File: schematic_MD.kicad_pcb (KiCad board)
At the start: 2 copper layers, 100 x 100 mm, 175 parts, among them J1 CAN_Bus, J10 XT60, J2 CAN_Bus, J3 Conn_02x01, J4 Micro_SD_Card_Det2, J5 Conn_02x07_Odd_Even, J6 Rotaly_encoder_1, J7 Rotaly_encoder_2, J8 XT60, J9 XT60, Q1 SQJ886EP-T1_GE3, Q2 SQJ886EP-T1_GE3, Q3 SQJ886EP-T1_GE3, Q4 SQJ886EP-T1_GE3, Q5 SQJ886EP-T1_GE3, Q6 SQJ886EP-T1_GE3, Q7 SQJ886EP-T1_GE3, Q8 SQJ886EP-T1_GE3, SW1 SW_MEC_5G, SW2 SW_DIP_x04, U1 74HC04, U2 MAX3051, U3 STM32F405RGTx, U4 UCC21520DW, U5 UCC21520DW, U6 UCC21520DW, U7 UCC21520DW, U8 TPS54202DDC, U9 XC6206P332MR-G, Y1 25MHz

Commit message: minor change
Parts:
- removed J4: Micro_SD_Card_Det2, RDC_footprint:TF-15
- added C60: 0.1u, Capacitor_SMD:C_0402_1005Metric, F.Cu at (80.9, 70.0)
- added J11: Micro_SD_Card_Det_Hirose_DM3AT, Connector_Card:microSD_HC_Hirose_DM3D-SF, F.Cu at (113.5, 132.8)
- added R62: 10k, Resistor_SMD:R_0402_1005Metric, F.Cu at (78.0, 70.0)
- added R63: 10k, Resistor_SMD:R_0402_1005Metric, F.Cu at (78.0, 72.0)
- moved R55 12.3 mm to (108.2, 124.2)
- moved R61 10.3 mm to (109.2, 124.2)
- moved R51 8.70 mm to (118.2, 124.2)
- moved R56 8.70 mm to (119.2, 124.2)
- moved R54 7.30 mm to (110.2, 124.2)
- moved R60 7.30 mm to (111.2, 124.2)
- moved R57 5.70 mm to (117.2, 124.2)
- moved R52 3.70 mm to (116.2, 124.2)
- moved R53 3.30 mm to (112.2, 124.2)
- moved R59 3.30 mm to (113.2, 124.2)
- moved R58 1.70 mm to (115.2, 124.2)
- moved C59 0.30 mm to (114.2, 124.2)
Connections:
- C16 pad 1: /STM32F405/3.3V_IN -> +3.3V
- C17 pad 1: /STM32F405/3.3V_IN -> +3.3V
- C19 pad 1: /STM32F405/3.3V_IN -> +3.3V
- C21 pad 1: /STM32F405/3.3V_IN -> +3.3V
- C22 pad 1: /STM32F405/3.3V_IN -> +3.3V
- C23 pad 1: /STM32F405/3.3V_IN -> +3.3V
- C52 pad 1: +12V -> /Logic_power/Power_IN
- C53 pad 1: +12V -> /Logic_power/Power_IN
- L1 pad 1: /STM32F405/3.3V_IN -> +3.3V
- SW2 pad 5: /STM32F405/3.3V_IN -> +3.3V
- SW2 pad 6: /STM32F405/3.3V_IN -> +3.3V
- SW2 pad 7: /STM32F405/3.3V_IN -> +3.3V
- SW2 pad 8: /STM32F405/3.3V_IN -> +3.3V
- U3 pad 1: /STM32F405/3.3V_IN -> +3.3V
- U3 pad 19: /STM32F405/3.3V_IN -> +3.3V
- U3 pad 32: /STM32F405/3.3V_IN -> +3.3V
- U3 pad 48: /STM32F405/3.3V_IN -> +3.3V
- U3 pad 64: /STM32F405/3.3V_IN -> +3.3V
- U8 pad 3: +12V -> /Logic_power/Power_IN
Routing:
- net +3.3V: track 127.0 -> 150.9 mm, vias 6 -> 14
- net /STM32F405/3.3V_IN: track 10.5 -> 0.00 mm
- net /STM32F405/D1: track 51.6 -> 58.6 mm
- net /STM32F405/D2: track 51.8 -> 44.8 mm
- net /STM32F405/D0: track 53.8 -> 58.8 mm
- net /STM32F405/D3: track 49.9 -> 45.3 mm
- net /STM32F405/SDCMD: track 47.4 -> 45.4 mm
- net /STM32F405/SDCLK: track 46.0 -> 47.1 mm, vias 4 -> 6
- net Net-(J11-DAT1): track 3.84 -> 4.62 mm
- net GND1: track 70.6 -> 71.1 mm
- net Net-(J11-CMD): track 3.87 -> 4.41 mm

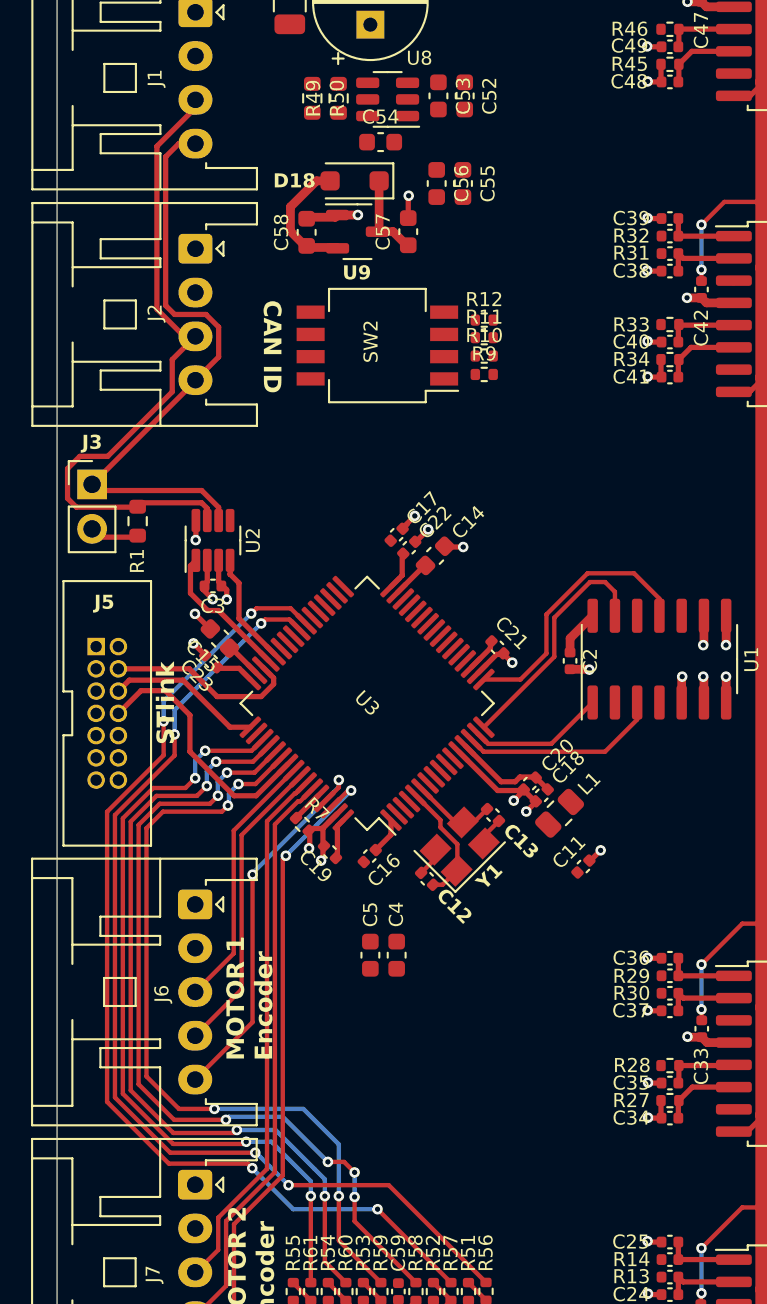
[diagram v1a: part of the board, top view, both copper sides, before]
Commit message: change logic DCDC
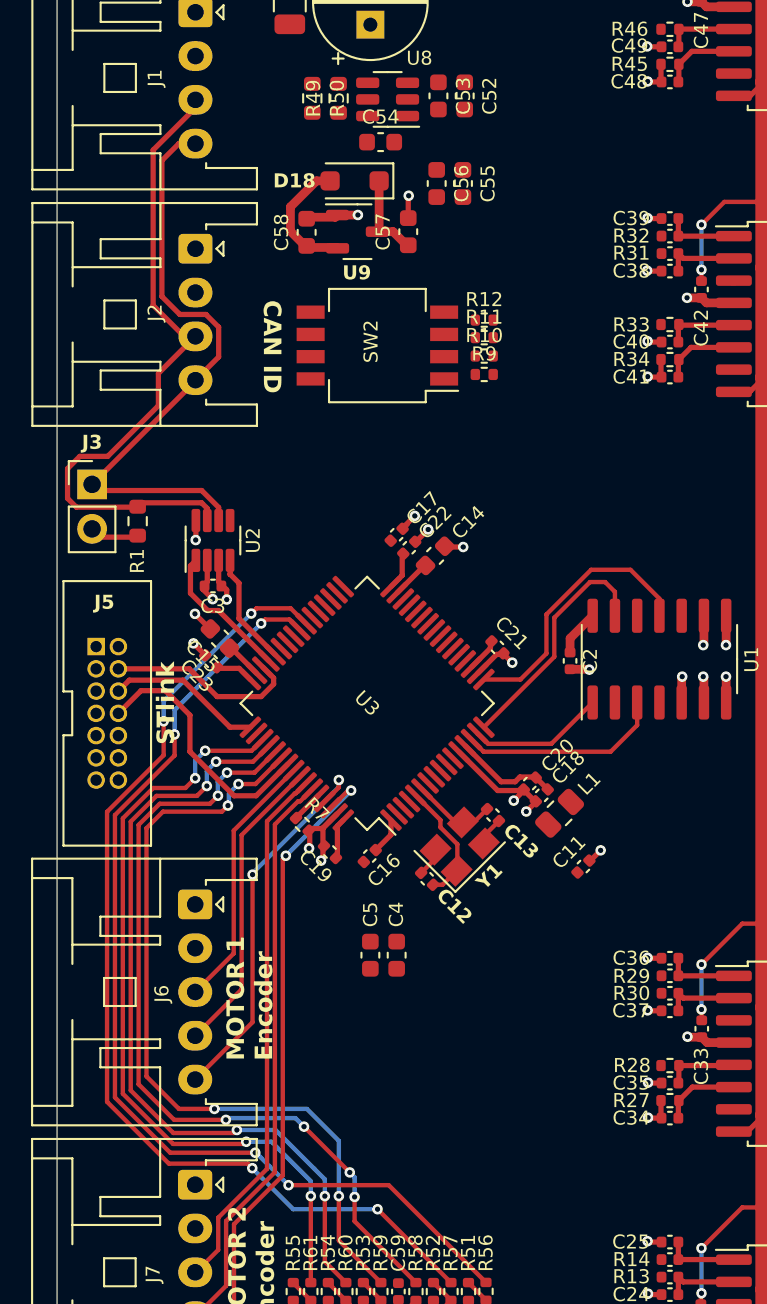
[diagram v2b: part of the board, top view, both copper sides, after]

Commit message: 制御回路完成
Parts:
- added C61: 220u, Capacitor_THT:CP_Radial_D8.0mm_P3.50mm, F.Cu at (141.8, 93.7)
- added C62: 0.1u, Capacitor_SMD:C_0603_1608Metric, F.Cu at (109.8, 113.9)
- added D19: D_Schottky, Diode_SMD:D_SOD-123F, F.Cu at (116.3, 50.9)
- added D20: D_Schottky, Diode_SMD:D_SOD-123F, F.Cu at (138.4, 79.2)
- added L2: 15uH, Inductor_SMD:L_Changjiang_FNR4020S, F.Cu at (118.1, 58.5)
- added L3: 15uH, Inductor_SMD:L_Changjiang_FNR4020S, F.Cu at (140.4, 86.9)
- added Q9: Q_PMOS_GSD, Package_TO_SOT_SMD:SOT-23-3, F.Cu at (109.5, 67.9)
- added R64: 18k, Resistor_SMD:R_0402_1005Metric, F.Cu at (144.2, 85.5)
- added R65: 2k, Resistor_SMD:R_0402_1005Metric, F.Cu at (145.2, 85.5)
- added R66: 10k, Resistor_SMD:R_0402_1005Metric, F.Cu at (120.5, 123.9)
- added R67: 10k, Resistor_SMD:R_0402_1005Metric, F.Cu at (133.2, 133.4)
- added SW3: SW_Push, RDC_footprint:TVBP06-B043, F.Cu at (132.6, 135.8)
- added SW4: SW_SPDT, RDC_footprint:SS-12D, F.Cu at (127.9, 42.8)
- added U10: TPS5430DDA, Package_SO:TI_SO-PowerPAD-8_ThermalVias, F.Cu at (120.3, 52.3)
- C1: value 100u -> 47u; footprint Capacitor_THT:CP_Radial_D6.3mm_P2.50mm -> Capacitor_THT:CP_Radial_D5.0mm_P2.00mm
- C53: value 0.1u -> 220u; footprint Capacitor_SMD:C_0603_1608Metric -> Capacitor_THT:CP_Radial_D8.0mm_P3.50mm
- C54: value 0.1u -> 0.01u
- C55: value 22u -> 10u
- C56: value 22u -> 0.01u
- R49: value 15k -> 12k; footprint Resistor_SMD:R_0603_1608Metric -> Resistor_SMD:R_0402_1005Metric
- R50: value 10k -> 3.9k; footprint Resistor_SMD:R_0603_1608Metric -> Resistor_SMD:R_0402_1005Metric
- SW1: value SW_MEC_5G -> SW_Push
- U8: value TPS54202DDC -> TPS5430DDA; footprint Package_TO_SOT_SMD:SOT-23-6 -> Package_SO:TI_SO-PowerPAD-8_ThermalVias
- moved R12 48.0 mm to (117.4, 116.7), turned to -90 degrees
- moved R11 47.0 mm to (116.4, 116.7), turned to -90 degrees
- moved R10 46.1 mm to (115.3, 116.7), turned to -90 degrees
- moved R9 45.1 mm to (114.3, 116.7), turned to -90 degrees
- moved SW2 40.5 mm to (115.9, 110.6), turned to 90 degrees
- moved U8 37.9 mm to (142.4, 80.8), turned to 90 degrees
- moved R62 31.9 mm to (109.9, 70.7), turned to 90 degrees
- moved C56 31.5 mm to (138.1, 83.8), turned to 0 degrees
- moved R63 30.9 mm to (108.9, 70.7), turned to -90 degrees
- moved C55 28.9 mm to (142.4, 76.2), turned to 0 degrees
- moved C60 27.0 mm to (107.9, 70.7), turned to -90 degrees
- moved D18 15.8 mm to (119.3, 74.6), turned to 0 degrees
- moved C58 15.3 mm to (122.0, 71.7), turned to -90 degrees
- moved R2 14.7 mm to (109.7, 65.0), turned to 180 degrees
- moved R50 13.3 mm to (122.5, 57.1)
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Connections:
- C1 pad 1: +12V -> /Logic_power/Power_IN
- C2 pad 1: gate_logic_PWR -> +3.3V
- C53 pad 1: /Logic_power/Power_IN -> +5V
- C54 pad 1: Net-(U8-BOOT) -> Net-(U10-BOOT)
- C54 pad 2: +5V -> Net-(D19-K)
- C55 pad 1: +5V -> Vdrive
- C55 pad 2: GND1 -> GND2
- C56 pad 1: +5V -> Net-(U8-BOOT)
- C56 pad 2: GND1 -> Net-(D20-K)
- H1 pad 1: GND1 -> unconnected-(H1-Pad1)
- H2 pad 1: GND1 -> unconnected-(H2-Pad1)
- H3 pad 1: GND2 -> unconnected-(H3-Pad1)
- H4 pad 1: GND2 -> unconnected-(H4-Pad1)
- J11 pad 10: unconnected-(J11-DET_A-Pad10) -> SD_Detect
- J11 pad 9: unconnected-(J11-DET_B-Pad9) -> +3.3V
- R10 pad 1: Net-(U3-PB14) -> /STM32F405/CAN_ID2
- R11 pad 1: Net-(U3-PB13) -> /STM32F405/CAN_ID3
- R12 pad 1: Net-(U3-PB12) -> /STM32F405/CAN_ID4
- R2 pad 1: +12V -> /Logic_power/Power_IN
- R49 pad 2: Net-(U8-FB) -> Net-(U10-VSENSE)
- R50 pad 1: Net-(U8-FB) -> Net-(U10-VSENSE)
- R62 pad 2: GND1 -> Net-(SW4-B)
- R8 pad 1: Net-(U3-PA10) -> Net-(U3-PB12)
- R9 pad 1: Net-(U3-PB15) -> /STM32F405/CAN_ID1
- SW2 pad 1: Net-(U3-PB15) -> /STM32F405/CAN_ID1
- SW2 pad 2: Net-(U3-PB14) -> /STM32F405/CAN_ID2
- SW2 pad 3: Net-(U3-PB13) -> /STM32F405/CAN_ID3
- SW2 pad 4: Net-(U3-PB12) -> /STM32F405/CAN_ID4
- U1 pad 14: gate_logic_PWR -> +3.3V
- U1 pad 5: GND1 -> /STM32F405/ENABLE_1
- U1 pad 6: GND1 -> /Driver/EN_left
- U1 pad 8: GND1 -> /Driver1/EN_left
- U1 pad 9: GND1 -> /STM32F405/ENABLE_2
- U3 pad 10: unconnected-(U3-PC2-Pad10) -> /STM32F405/CAN_ID2
- U3 pad 11: unconnected-(U3-PC3-Pad11) -> /STM32F405/CAN_ID1
- U3 pad 20: unconnected-(U3-PA4-Pad20) -> SD_Detect
- U3 pad 21: unconnected-(U3-PA5-Pad21) -> Net-(U3-PA5)
- U3 pad 24: /Driver/EN_left -> /STM32F405/ENABLE_1
- U3 pad 25: /Driver1/EN_left -> /STM32F405/ENABLE_2
- U3 pad 34: Net-(U3-PB13) -> unconnected-(U3-PB13-Pad34)
- U3 pad 35: Net-(U3-PB14) -> unconnected-(U3-PB14-Pad35)
- U3 pad 36: Net-(U3-PB15) -> unconnected-(U3-PB15-Pad36)
- U3 pad 43: Net-(U3-PA10) -> unconnected-(U3-PA10-Pad43)
- U3 pad 8: unconnected-(U3-PC0-Pad8) -> /STM32F405/CAN_ID4
- U3 pad 9: unconnected-(U3-PC1-Pad9) -> /STM32F405/CAN_ID3
- U8 pad 1: GND1 -> Net-(U8-BOOT)
- U8 pad 2: Net-(U8-SW) -> unconnected-(U8-NC-Pad2)
- U8 pad 3: /Logic_power/Power_IN -> unconnected-(U8-NC-Pad3)
- U8 pad 4: Net-(U8-FB) -> Net-(U8-VSENSE)
- U8 pad 6: Net-(U8-BOOT) -> GND2
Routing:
- net +3.3V: track 150.9 -> 446.7 mm, vias 14 -> 46
- net +5V: track 5.06 -> 155.1 mm, vias 0 -> 12
- net Net-(SW4-B): track 0.00 -> 68.8 mm, vias 0 -> 6
- net Net-(U3-PB12): track 0.00 -> 66.6 mm, vias 0 -> 6
- net Net-(U3-PA5): track 0.00 -> 65.7 mm, vias 0 -> 2
- net /STM32F405/NRST: track 0.00 -> 51.5 mm, vias 0 -> 4
- net SD_Detect: track 0.00 -> 48.6 mm, vias 0 -> 4
- net /Driver/EN_left: track 8.34 -> 51.6 mm, vias 0 -> 4
- net /Driver1/EN_left: track 8.32 -> 50.2 mm, vias 0 -> 2
- net /Driver1/Right_Highside_PWM_IN: track 13.8 -> 54.0 mm, vias 0 -> 2
- net /Driver1/Right_Lowside_PWM_IN: track 0.00 -> 40.0 mm, vias 0 -> 2
- net /Driver/Left_Lowside_PWM_IN: track 0.00 -> 35.2 mm, vias 0 -> 2
- net /Driver/Left_Highside_PWM_IN: track 7.82 -> 42.9 mm, vias 0 -> 2
- net /STM32F405/CAN_ID1: track 0.00 -> 30.8 mm, vias 0 -> 2
- net /STM32F405/CAN_ID2: track 0.00 -> 29.2 mm, vias 0 -> 2
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- added copper zone on F.Cu, net +12V
- added copper zone on F.Cu, net +5V
- added copper zone on F.Cu, net /Logic_power/Power_IN
- added copper zone on B.Cu, net GND1
- added copper zone on F.Cu, net GND1
- added copper zone on F.Cu, net Net-(D19-K)
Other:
- outline, holes or cut-outs redrawn
- board text added: "CAN"

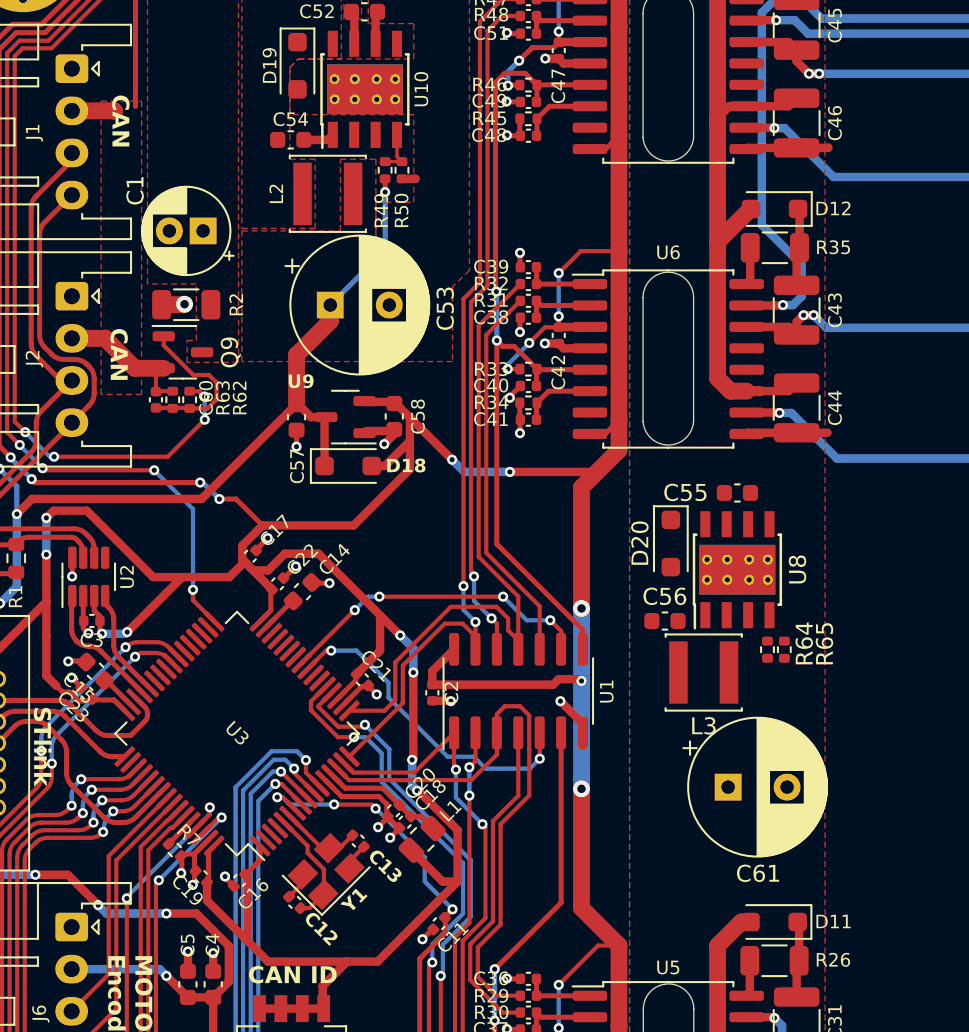
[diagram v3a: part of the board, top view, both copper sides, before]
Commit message: wired gate power
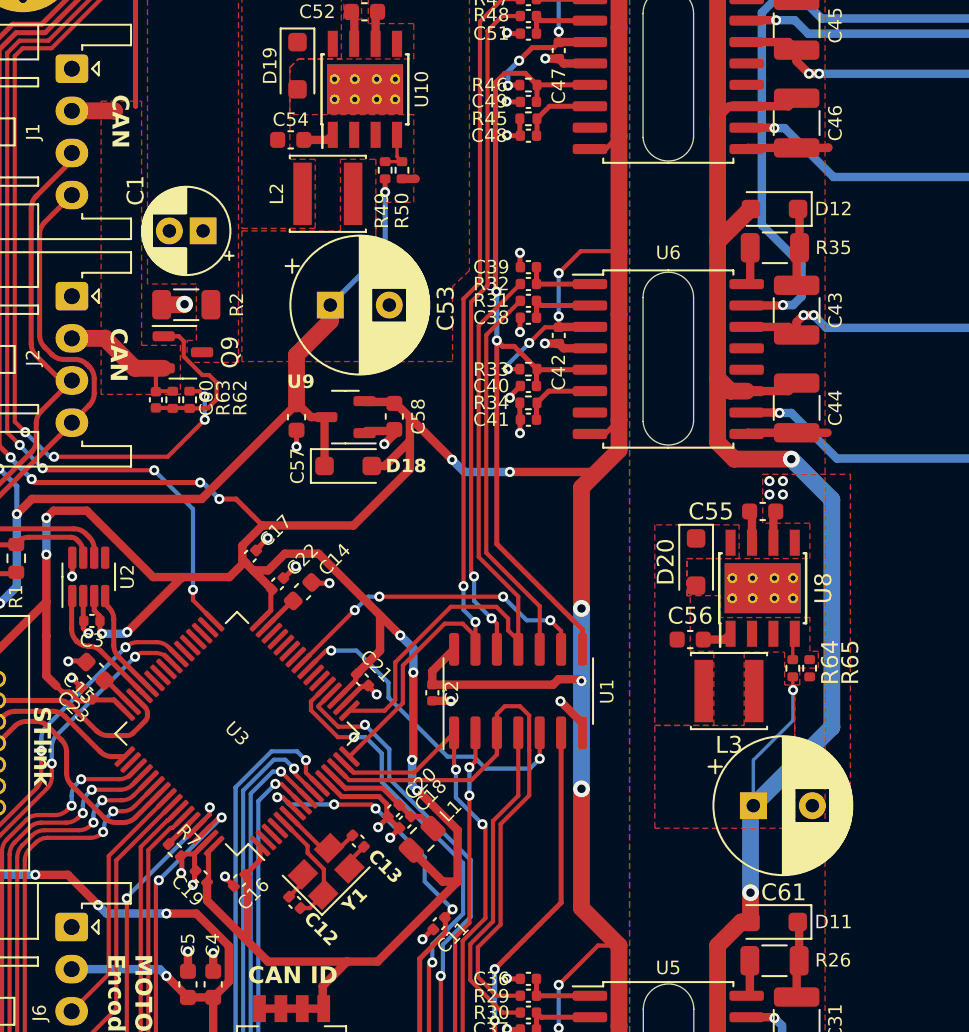
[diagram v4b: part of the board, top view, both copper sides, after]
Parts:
- moved C56 1.86 mm to (139.6, 84.9), turned to 180 degrees
- moved U8 1.86 mm to (143.9, 81.9)
- moved C55 1.86 mm to (143.9, 77.3)
- moved C61 1.86 mm to (143.3, 94.8)
- moved D20 1.86 mm to (139.9, 80.3)
- moved L3 1.86 mm to (141.9, 88.0)
- moved R64 1.86 mm to (145.7, 86.6)
- moved R65 1.86 mm to (146.7, 86.6)
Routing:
- net Gate_power: track 82.2 -> 129.8 mm, vias 0 -> 3
- net GND2: track 20.7 -> 22.6 mm, vias 1 -> 5
- net Vdrive: track 17.5 -> 19.4 mm
- net Net-(U8-BOOT): track 0.00 -> 1.76 mm
- net Net-(U8-VSENSE): track 0.00 -> 1.58 mm
- added copper zone on F.Cu, net Gate_power
- added copper zone on F.Cu, net Net-(D20-K)

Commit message: pre compleate
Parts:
- removed C10: 1uF, Capacitor_SMD:C_0603_1608Metric
- moved R24 0.40 mm to (170.0, 114.4)
- moved R22 0.30 mm to (168.5, 114.9)
- moved D7 0.25 mm to (169.8, 124.8)
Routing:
- net Vdrive: track 19.4 -> 75.9 mm, vias 155 -> 156
- net Net-(Q4-G): track 5.11 -> 3.24 mm
- net Net-(Q2-G): track 5.08 -> 3.22 mm
- net /Driver1/H-bridge_left: track 19.0 -> 19.7 mm
- net /Driver1/H-bridge_right: track 20.0 -> 20.6 mm
- net /Driver/H-bridge_left: track 20.4 -> 21.0 mm
- net /Driver/H-bridge_right: track 19.7 -> 20.1 mm, vias 5 -> 4
- net Gate_power: track 129.8 -> 130.1 mm, vias 3 -> 2
- added copper zone on B.Cu, net GND2

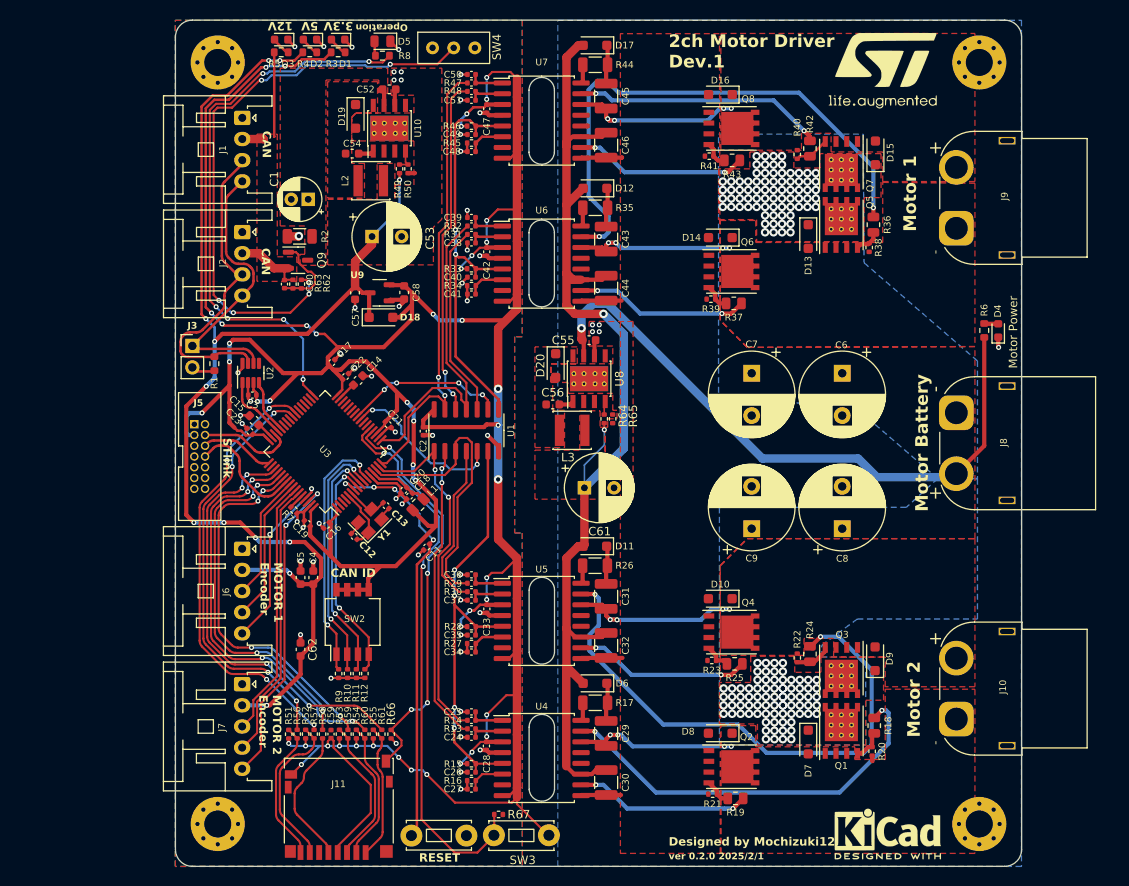
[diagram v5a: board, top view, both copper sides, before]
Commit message: DCDCコンバータ部分を修正
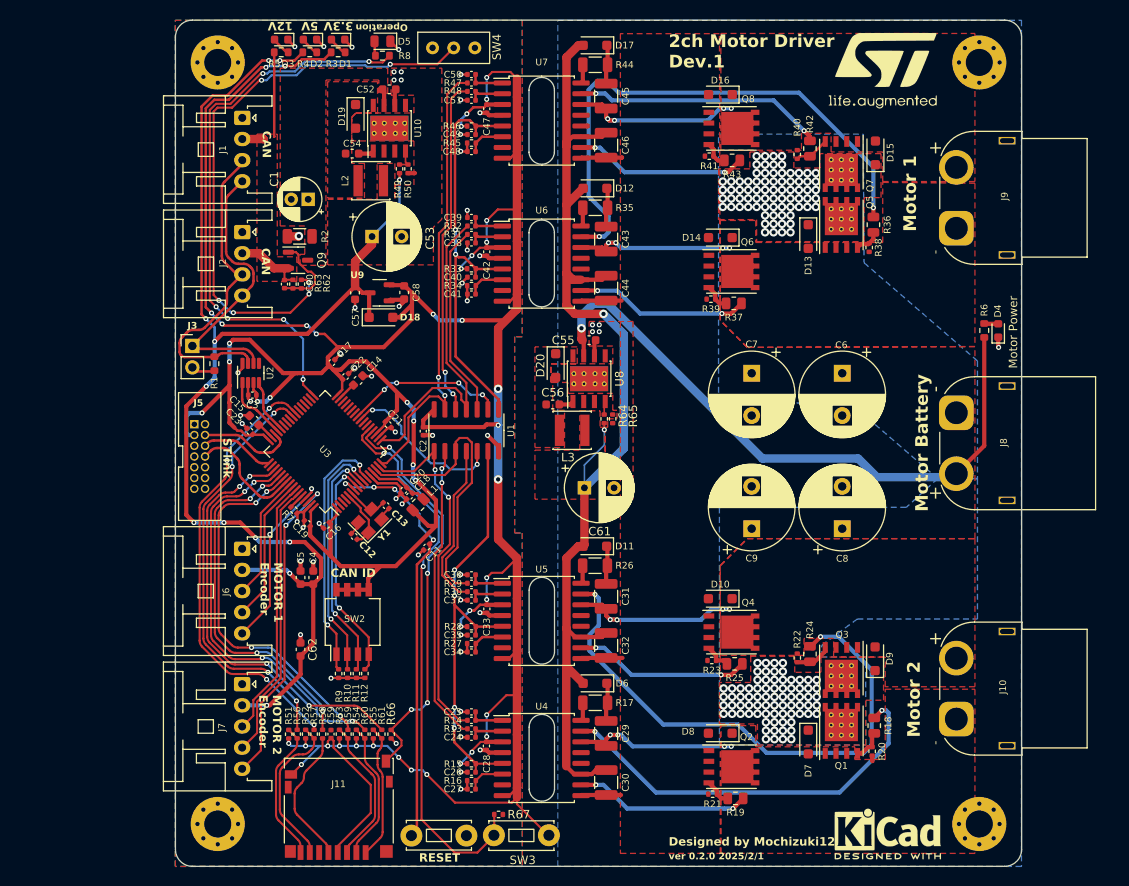
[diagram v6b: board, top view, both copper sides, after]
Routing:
- net Vdrive: vias 156 -> 153

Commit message: DRC 完了
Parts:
- moved SW3 0.06 mm to (132.7, 135.8)
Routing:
- net GND1: track 82.4 -> 85.4 mm, vias 52 -> 375
- net Gate_power: track 130.1 -> 127.6 mm
- net /STM32F405/NRST: track 51.5 -> 49.4 mm, vias 4 -> 2
- net Net-(U8-VSENSE): track 1.58 -> 2.58 mm
- net Vdrive: track 75.9 -> 76.5 mm
- net GND2: vias 5 -> 28
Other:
- board text added: "TEST"
- board text added: "制御電源"

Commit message: minor fix
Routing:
- net Vdrive: track 76.5 -> 77.1 mm
- net GND2: vias 28 -> 53
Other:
- board text added: "2ch Motor Driver Prot.2"
- board text added: "ver 0.2.0 2025/4/6"
- board text removed: "2ch Motor Driver Dev.1"
- board text removed: "ver 0.2.0 2025/2/1"
